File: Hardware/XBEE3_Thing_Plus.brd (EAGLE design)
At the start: 22.9 x 58.4 mm, 108 parts, among them Q1 2.5A/30V, U1 XBEE3_Micro, U2 MCP73831, U3 AP2112K-3.3V, U4 CP2102N

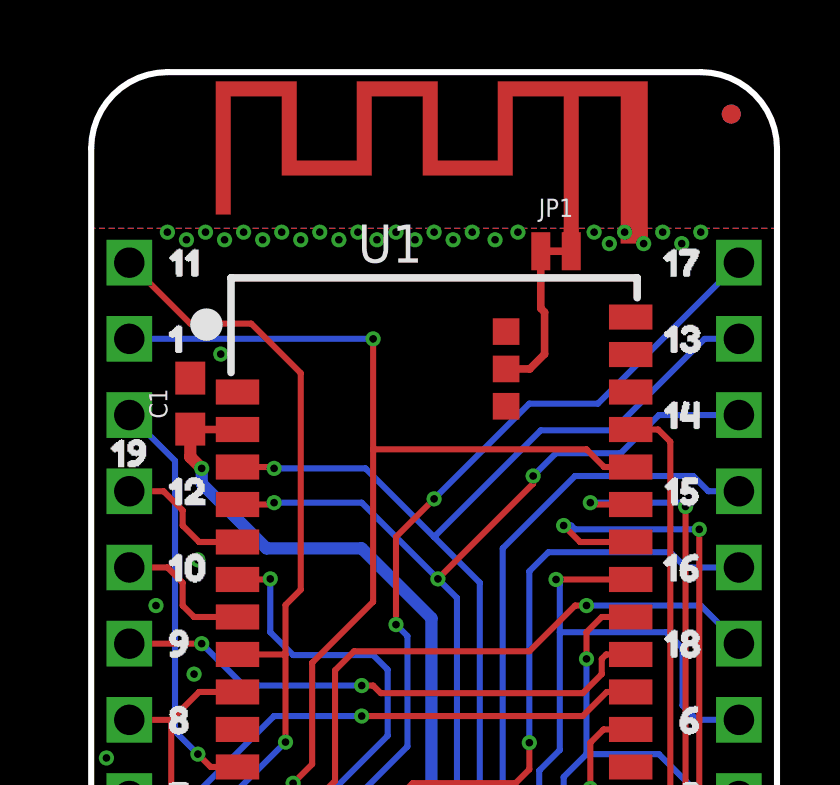
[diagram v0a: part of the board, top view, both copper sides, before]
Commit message: v01 update
Removed test points from bottom of the board, removed the trace antenna, and modified the top ground pour as outlined in the XBee3 datasheet
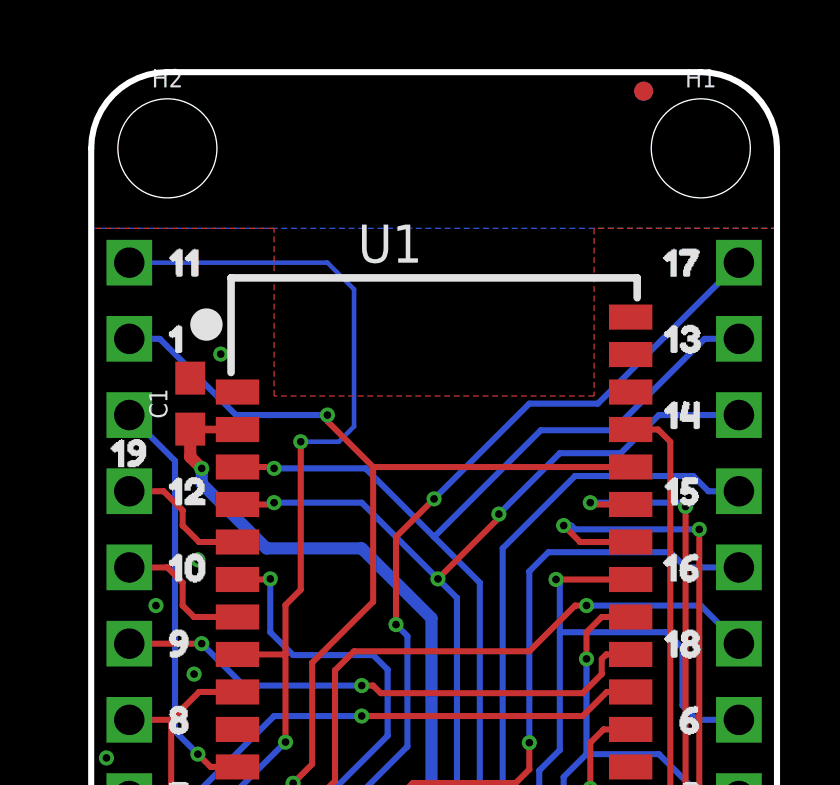
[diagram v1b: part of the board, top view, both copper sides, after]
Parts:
- removed E1: ANTENNA-GROUNDEDTRACE-15.2M_FLIPPED, SparkFun-RF:TRACE_ANTENNA_2.4GHZ_15.2MM_FLIPPED
- removed JP1: (no value), SparkFun-Jumpers:SMT-JUMPER_2_NC_TRACE_NO-SILK
- added H1, H2: STAND-OFF, SparkFun-Hardware:STAND-OFF
- moved FD3 3.02 mm to (18.4, 57.8)
- moved FD4 3.02 mm to (18.4, 57.8)
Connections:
- removed net N$1: E1.ANT, JP1.2
- removed net RF: JP1.1, U1.P$36
- net GND: no longer E1.GND, U1.P$35, U1.P$37
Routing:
- net RF: track 4.97 -> 0.00 mm
- net SDA: track 51.5 -> 56.4 mm, vias 2 -> 3
- net SCL: track 62.2 -> 59.6 mm
- net N$1: track 0.51 -> 0.00 mm
- net GND: vias 42 -> 16

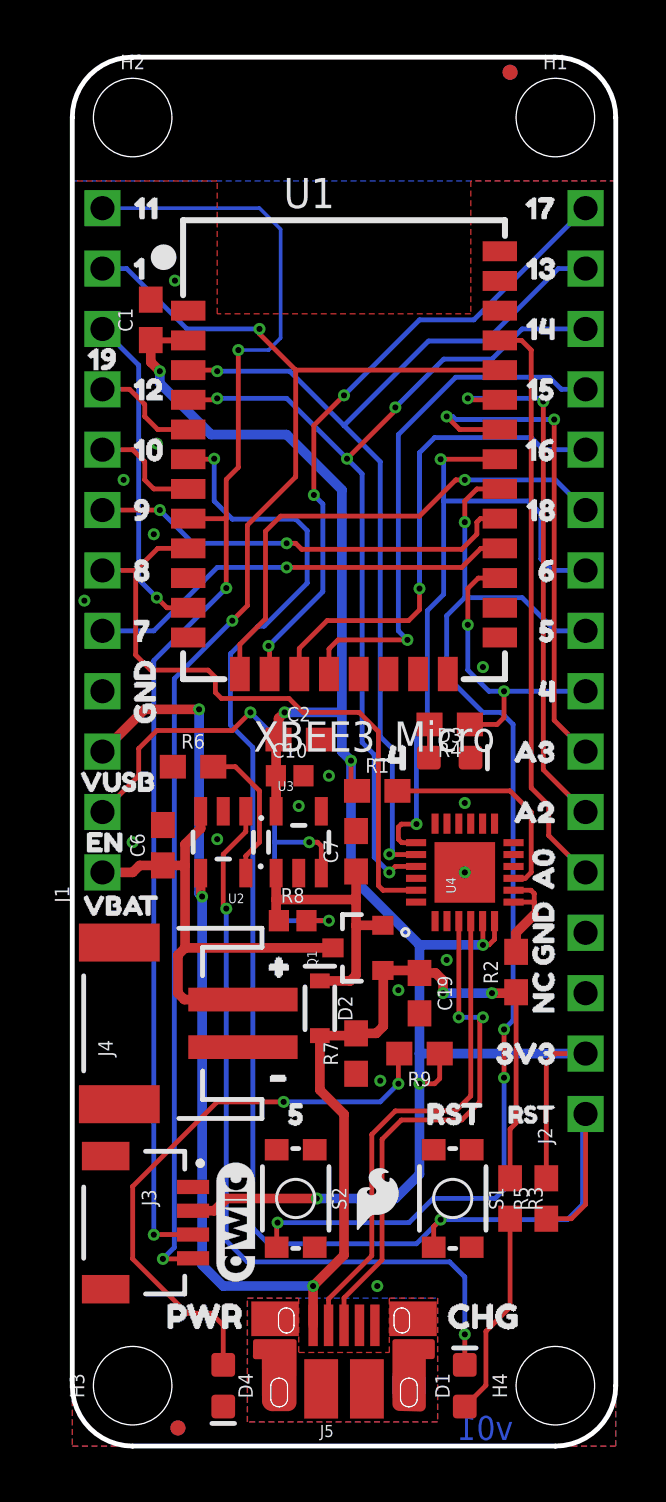
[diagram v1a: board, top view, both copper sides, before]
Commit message: v01 Design Review Changes
- Adjusted R2
- Modified bottom ground pour
- Swapped D17 and extra ground header pads
- Updated buzzard labels
- Rotated name and logo on bottom
- Added SparkFun name logo to top of board
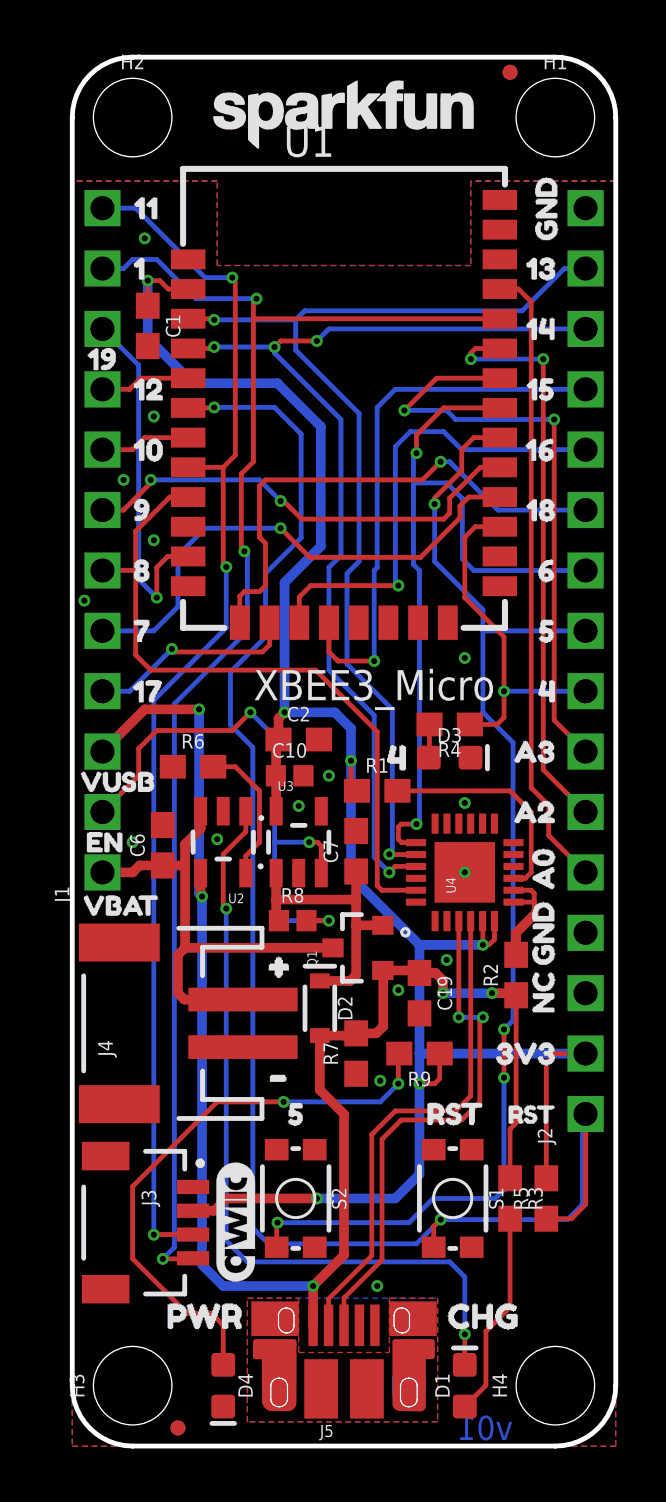
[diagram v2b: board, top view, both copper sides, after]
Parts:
- U$16: device buzzard_labels (17):17#CS15 -> buzzard_labels (17):GND3
- U$20: device buzzard_labels (17):GND3 -> SparkFun-Aesthetics:SFE_LOGO_NAME_.1
- U$53: device buzzard_labels (18):GND12 -> buzzard_labels (23):17##CS0
- U$62: device SparkFun-Aesthetics:SFE_LOGO_FLAME_.1 -> buzzard_labels (18):GND12
- moved U$62 40.1 mm to (19.9, 49.9), turned to 90 degrees
- moved U$65 31.8 mm to (13.7, 40.3), turned to 270 degrees
- moved U$29 26.2 mm to (1.78, 31.8)
- moved U$20 24.8 mm to (11.4, 56.0), flipped to the top
- moved LOGO1 19.9 mm to (10.8, 31.4), turned to 270 degrees
- moved U$53 4.16 mm to (6.60, 31.8), flipped to the bottom, turned to 0 degrees
- moved U1 2.16 mm to (11.4, 44.1)
- moved C1 0.28 mm to (3.17, 47.1), turned to 270 degrees
- moved LOGO2 0.18 mm to (11.4, 20.2), turned to 270 degrees
- moved R2 0.13 mm to (18.7, 19.8)
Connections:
- net VIN renamed N$1
- removed net SS: J2.16, U1.P$14
- new net D17: J1.4, U1.P$14
- net GND: now also J2.16; no longer J1.4
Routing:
- net SS: track 26.8 -> 0.00 mm, vias 3 -> 0
- net D17: track 0.00 -> 8.88 mm, vias 0 -> 1
- net SDA: track 56.4 -> 51.7 mm
- net 3.3V: track 82.2 -> 86.4 mm
- net D6: track 28.8 -> 32.9 mm
- net A3: track 21.6 -> 25.5 mm
- net D7: track 18.2 -> 21.6 mm
- net TX: track 39.5 -> 42.8 mm
- net RX: track 40.5 -> 43.4 mm
- net A0: track 24.4 -> 26.5 mm
- net D4: track 12.9 -> 14.9 mm, vias 2 -> 1
- net A2: track 22.6 -> 24.4 mm
- net !RST: track 64.2 -> 65.9 mm
- net SCL: track 59.6 -> 61.2 mm
- net D8: track 27.6 -> 29.1 mm
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
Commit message: v10
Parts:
- removed U$10: (no value), buzzard_labels (17):6##RTS9
- removed U$22: (no value), buzzard_labels (17):8##DTR20
- removed U$53: (no value), buzzard_labels (23):17##CS0
- added U$67: (no value), buzzard_labels (3):6#0
- added U$68: (no value), buzzard_labels (3):#RTS1
- added U$69: (no value), buzzard_labels (3):#DTR3
- added U$70: (no value), buzzard_labels (3):8#2
- added U$71: (no value), buzzard_labels (3):17#4
- added U$72: (no value), buzzard_labels (3):#CS5
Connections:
- net RX renamed D13
- net SCL renamed D1
- net SDA renamed D11
- net TX renamed D14
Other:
- board text added: "v10"
- board text removed: "v01"
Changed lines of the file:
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@@
 <wire x1="16.383" y1="25.50668125" x2="16.637" y2="25.50668125" width="0.2032" layer="41"/>
 <wire x1="17.88668125" y1="24.003" x2="17.88668125" y2="24.257" width="0.2032" layer="41"/>
-<text x="18.542" y="0.254" size="1.016" layer="16" font="vector" ratio="15" rot="MR0">v01</text>
+<text x="18.542" y="0.254" size="1.016" layer="16" font="vector" ratio="15" rot="MR0">v10</text>
 <text x="14.097" y="-19.177" size="1.778" layer="51">Alex Wende</text>
 <dimension x1="2.54" y1="2.54" x2="0" y2="2.54" x3="1.27" y3="-3.81" textsize="1.016" layer="47" unit="inch"/>
@@
 <element name="U$8" library="buzzard_labels (17)" package="47" value="" x="21.463" y="31.75" smashed="yes" rot="MR0"/>
 <element name="U$9" library="buzzard_labels (17)" package="58" value="" x="21.463" y="34.29" smashed="yes" rot="MR0"/>
-<element name="U$10" library="buzzard_labels (17)" package="6##RTS9" value="" x="21.6535" y="36.83" smashed="yes" rot="MR0"/>
 <element name="U$11" library="buzzard_labels (17)" package="18#SCK10" value="" x="21.463" y="39.37" smashed="yes" rot="MR0"/>
 <element name="U$12" library="buzzard_labels (17)" package="16#MOSI11" value="" x="21.5265" y="41.91" smashed="yes" rot="MR0"/>
@@
 <element name="U$19" library="buzzard_labels (17)" package="VUSB18" value="" x="6.985" y="29.21" smashed="yes" rot="MR0"/>
 <element name="U$21" library="buzzard_labels (17)" package="719" value="" x="3.937" y="34.29" smashed="yes" rot="MR0"/>
-<element name="U$22" library="buzzard_labels (17)" package="8##DTR20" value="" x="6.985" y="36.83" smashed="yes" rot="MR0"/>
 <element name="U$23" library="buzzard_labels (17)" package="921" value="" x="3.81" y="39.37" smashed="yes" rot="MR0"/>
 <element name="U$24" library="buzzard_labels (17)" package="1022" value="" x="4.572" y="41.91" smashed="yes" rot="MR0"/>
@@
 </element>
 <element name="U$20" library="SparkFun-Aesthetics" package="SFE_LOGO_NAME_.1" value="" x="11.43" y="56.007" smashed="yes"/>
-<element name="U$53" library="buzzard_labels (23)" package="17##CS0" value="" x="6.604" y="31.75" smashed="yes" rot="MR0"/>
 <element name="U$16" library="buzzard_labels (17)" package="GND3" value="" x="21.463" y="52.07" smashed="yes" rot="MR0"/>
 <element name="U$62" library="buzzard_labels (18)" package="GND12" value="" x="19.939" y="49.911" smashed="yes" rot="R90"/>
+<element name="U$67" library="buzzard_labels (3)" package="6#0" value="" x="21.463" y="36.83" smashed="yes" rot="MR0"/>
+<element name="U$68" library="buzzard_labels (3)" package="#RTS1" value="" x="19.558" y="36.83" smashed="yes" rot="MR0"/>
+<element name="U$69" library="buzzard_labels (3)" package="#DTR3" value="" x="5.715" y="36.83" smashed="yes" rot="MR0"/>
+<element name="U$70" library="buzzard_labels (3)" package="8#2" value="" x="7.62" y="36.83" smashed="yes" rot="MR0"/>
+<element name="U$71" library="buzzard_labels (3)" package="17#4" value="" x="7.239" y="31.75" smashed="yes" rot="MR0"/>
+<element name="U$72" library="buzzard_labels (3)" package="#CS5" value="" x="4.826" y="31.75" smashed="yes" rot="MR0"/>
 </elements>
 <signals>
@@
 <wire x1="3.048" y1="42.418" x2="2.54" y2="41.91" width="0.2032" layer="1"/>
 </signal>
-<signal name="SDA">
+<signal name="D11">
 <contactref element="U1" pad="P$8"/>
 <contactref element="J3" pad="3"/>
 <contactref element="J1" pad="12"/>
-<wire x1="6.35" y1="41.16831875" x2="6.35" y2="37.10431875" width="0.2032" layer="1"/>
-<wire x1="6.35" y1="37.10431875" x2="6.477" y2="36.97731875" width="0.2032" layer="1"/>
+<wire x1="6.35" y1="41.16831875" x2="6.35" y2="37.23131875" width="0.2032" layer="1"/>
+<wire x1="6.35" y1="37.23131875" x2="6.858" y2="36.72331875" width="0.2032" layer="1"/>
 <wire x1="6.35" y1="41.16831875" x2="6.858" y2="41.67631875" width="0.2032" layer="1"/>
 <wire x1="6.731" y1="49.149" x2="6.858" y2="49.149" width="0.2032" layer="1"/>
@@
 <wire x1="3.429" y1="8.898" x2="3.429" y2="8.89" width="0.2032" layer="1"/>
 <via x="3.429" y="8.89" extent="1-16" drill="0.254"/>
-<via x="6.477" y="36.97731875" extent="1-16" drill="0.254"/>
+<via x="6.858" y="36.72331875" extent="1-16" drill="0.254"/>
 <wire x1="3.429" y1="31.369" x2="3.429" y2="8.89" width="0.2032" layer="16"/>
 <via x="6.731" y="49.149" extent="1-16" drill="0.254"/>
 <wire x1="4.8768" y1="41.16831875" x2="6.35" y2="41.16831875" width="0.2032" layer="1"/>
 <wire x1="3.429" y1="31.369" x2="6.477" y2="34.417" width="0.2032" layer="16"/>
-<wire x1="6.477" y1="34.417" x2="6.477" y2="36.97731875" width="0.2032" layer="16"/>
+<wire x1="6.477" y1="36.34231875" x2="6.477" y2="34.417" width="0.2032" layer="16"/>
+<wire x1="6.477" y1="36.34231875" x2="6.858" y2="36.72331875" width="0.2032" layer="16"/>
 <wire x1="1.27" y1="52.07" x2="2.667" y2="52.07" width="0.2032" layer="16"/>
 <wire x1="5.588" y1="49.149" x2="6.731" y2="49.149" width="0.2032" layer="16"/>
 <wire x1="5.588" y1="49.149" x2="2.667" y2="52.07" width="0.2032" layer="16"/>
 </signal>
-<signal name="SCL">
+<signal name="D1">
 <contactref element="U1" pad="P$30"/>
 <contactref element="J3" pad="4"/>
@@
 <wire x1="19.304" y1="26.67" x2="18.415" y2="27.559" width="0.2032" layer="1"/>
 </signal>
-<signal name="RX">
+<signal name="D13">
 <contactref element="U4" pad="20"/>
 <contactref element="U1" pad="P$3"/>
@@
 <wire x1="9.398" y1="46.101" x2="9.398" y2="47.371" width="0.2032" layer="16"/>
 </signal>
-<signal name="TX">
+<signal name="D14">
 <contactref element="U4" pad="21"/>
 <contactref element="U1" pad="P$4"/>
